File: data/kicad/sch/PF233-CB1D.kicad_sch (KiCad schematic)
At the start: 70 parts, among them M5 5 V 1.5 A switching module, U1 Pico 2 W

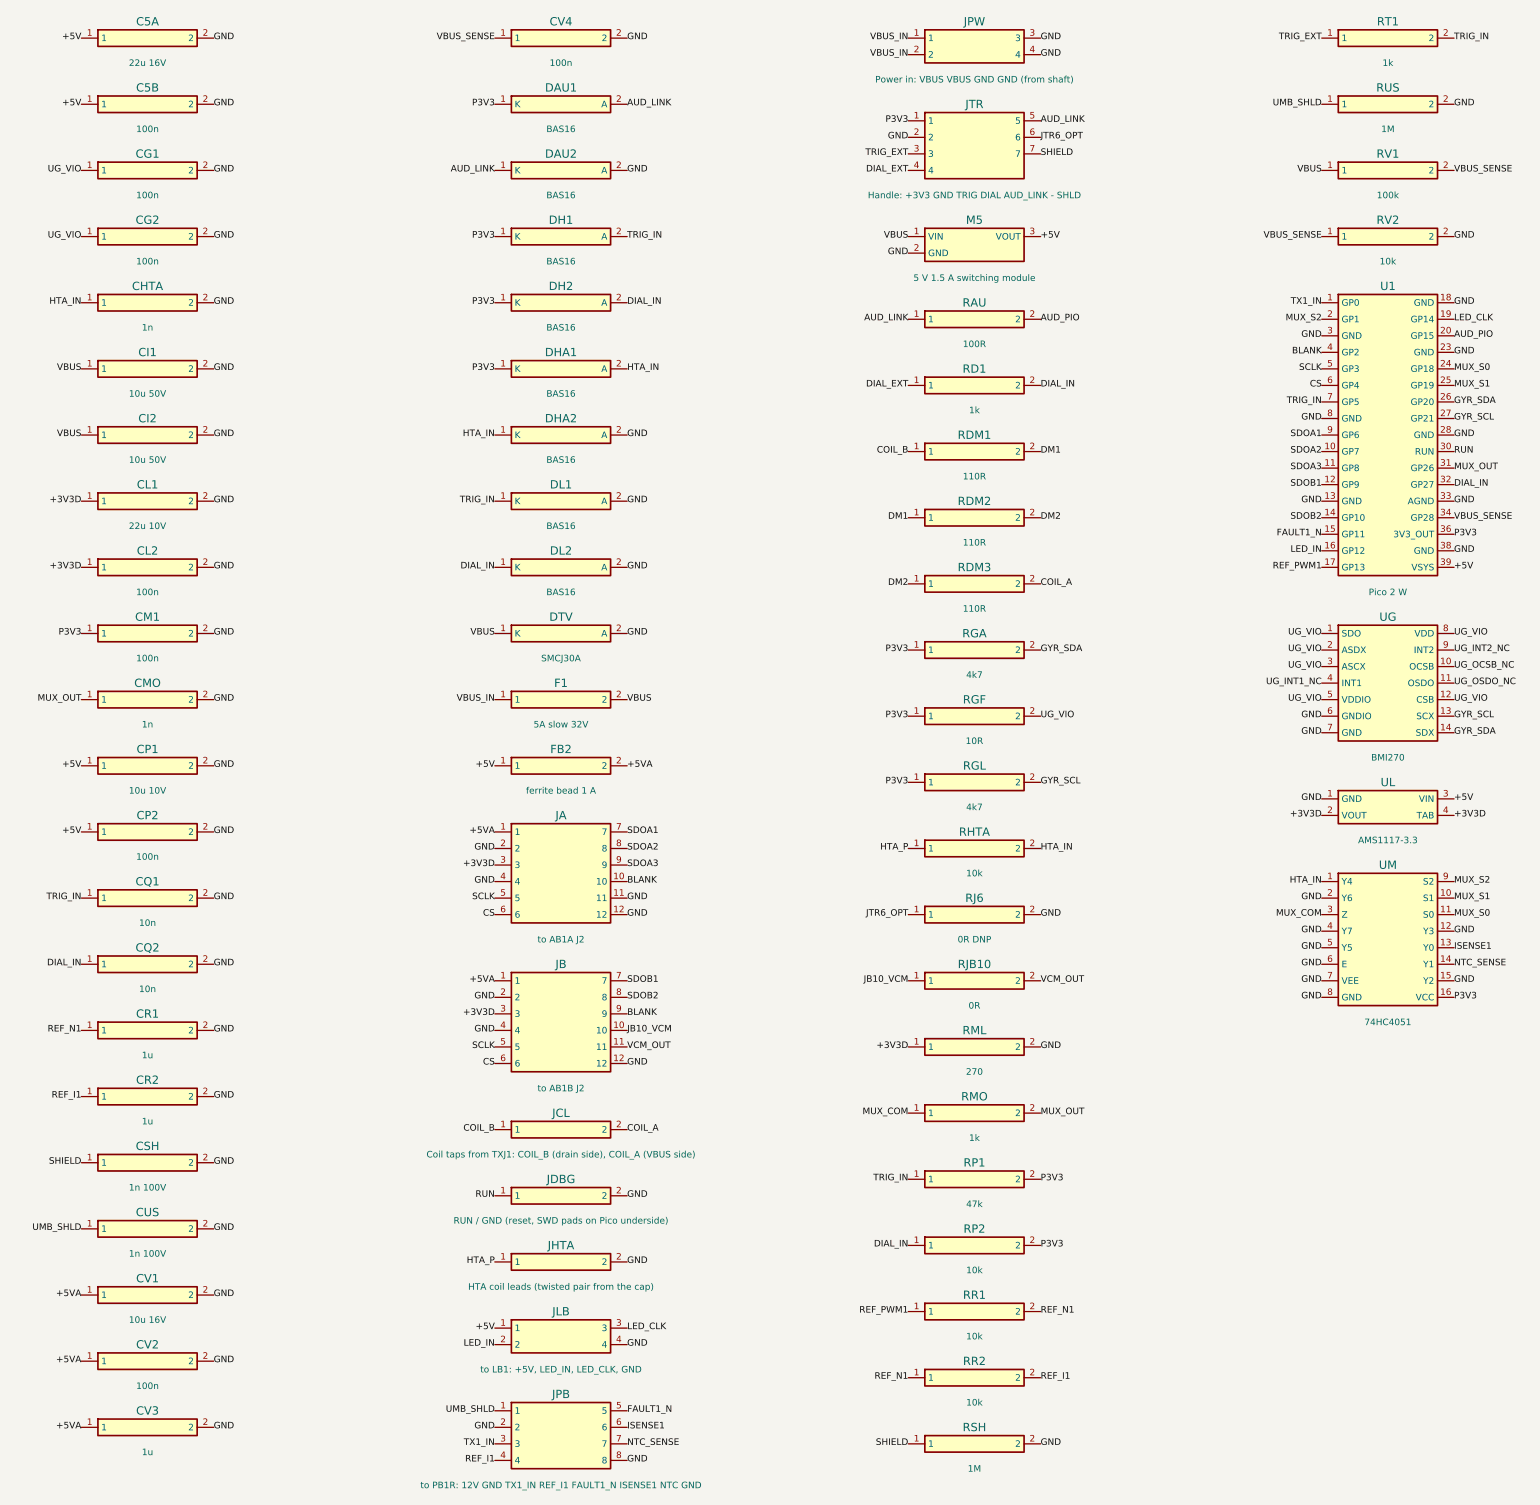
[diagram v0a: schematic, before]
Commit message: WIP (NOT signed off): sign-off outputs with AU1 38 / 38 (exact DRC 0 / 0, all AU1 checks pass); CB1D 45 / 46 (TRIG_EXT open on the 0.125 grid, being re-routed on 0.15)
Co-Authored-By: Claude Opus 5.5 <noreply@anthropic.com>
Claude-Session: https://claude.ai/code/session_01FX4DWSYYjMCFGGA6gmha65
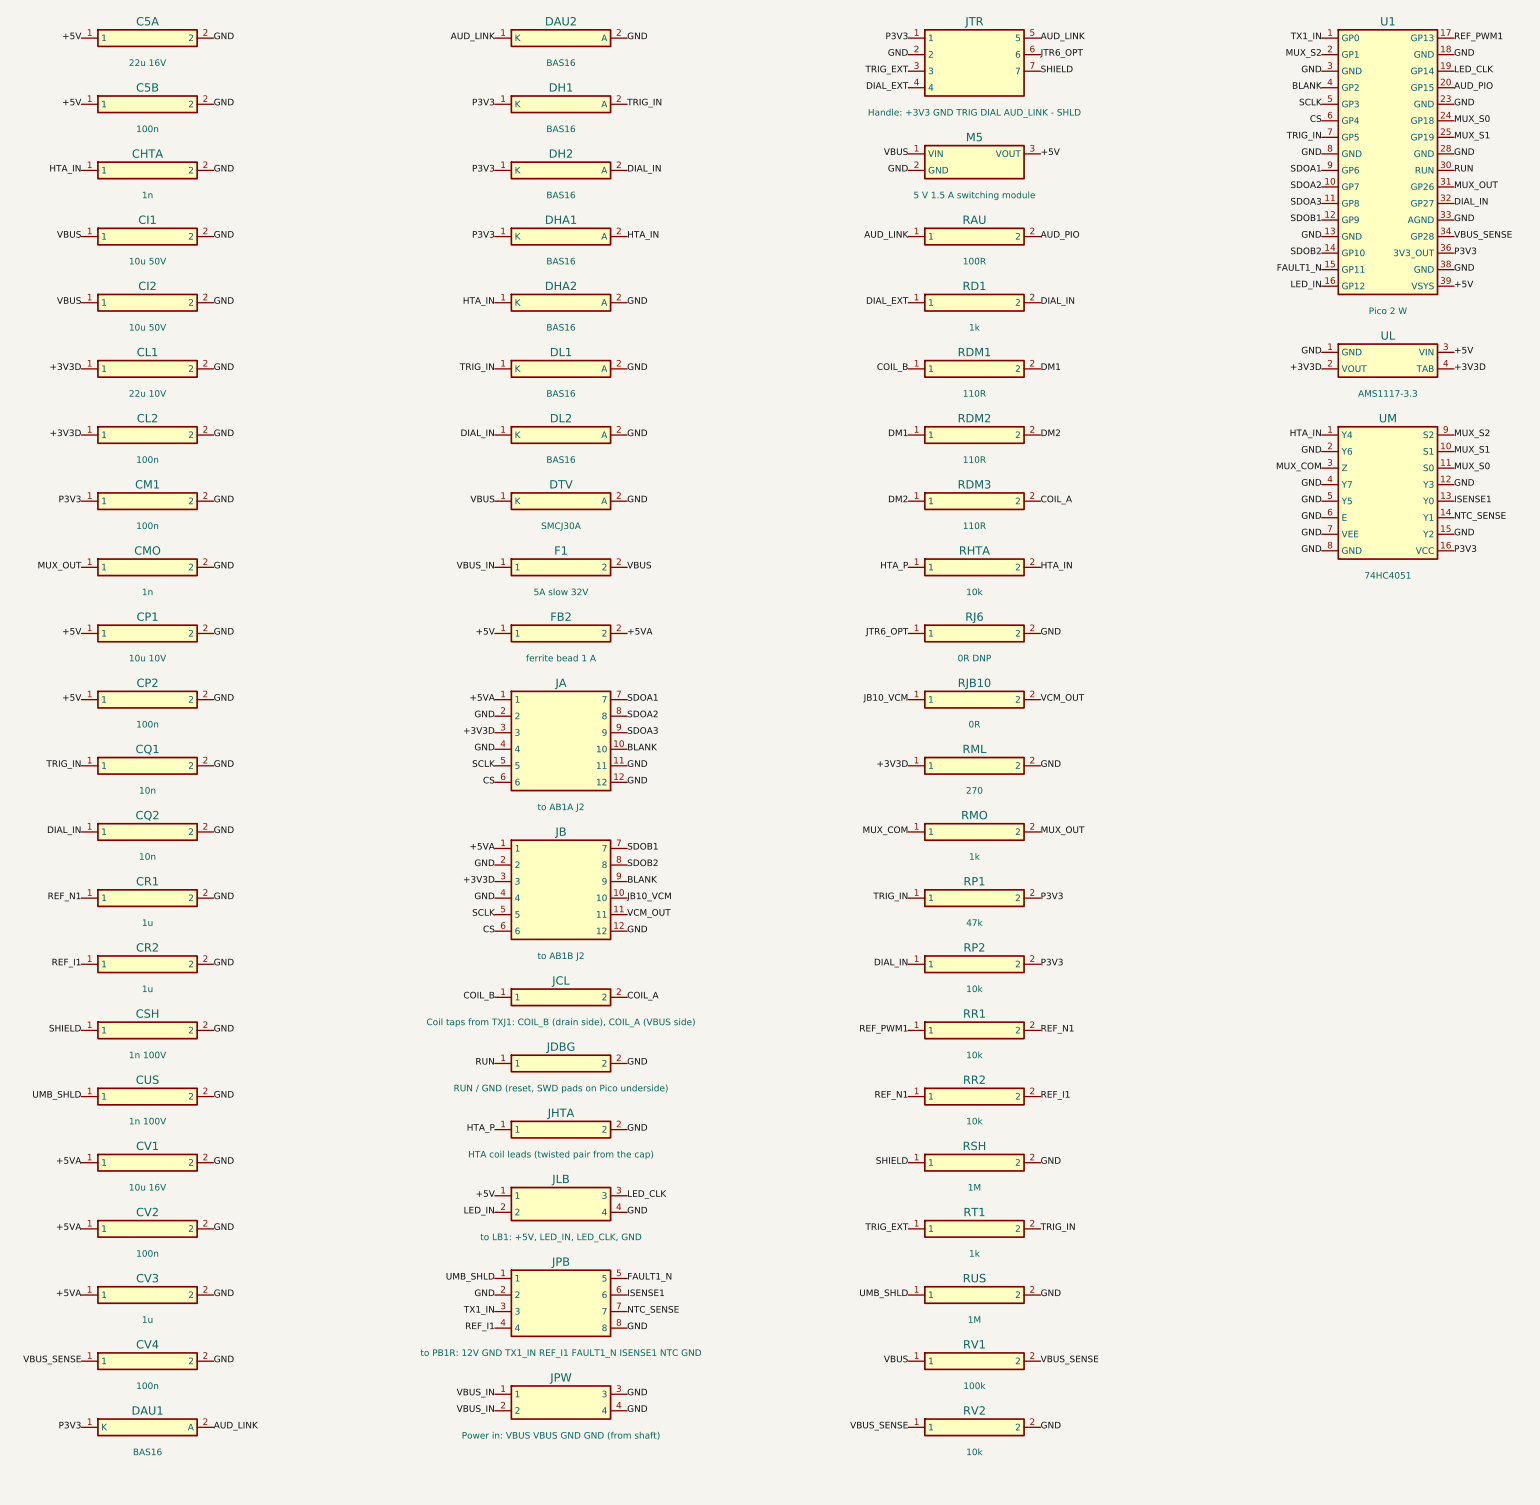
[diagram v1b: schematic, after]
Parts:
- removed CG1: 100n, Capacitor_SMD:C_0603_1608Metric, symbol PF233_auto:CG1
- removed CG2: 100n, Capacitor_SMD:C_0603_1608Metric, symbol PF233_auto:CG2
- removed RGA: 4k7, Resistor_SMD:R_0603_1608Metric, symbol PF233_auto:RGA
- removed RGF: 10R, Resistor_SMD:R_0603_1608Metric, symbol PF233_auto:RGF
- removed RGL: 4k7, Resistor_SMD:R_0603_1608Metric, symbol PF233_auto:RGL
- removed UG: BMI270, PF233:BMI270_LGA-14_2.5x3.0mm, symbol PF233_auto:UG
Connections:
- removed net GYR_SCL: U1.27 (GP21)
- removed net GYR_SDA: U1.26 (GP20)
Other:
- moved on the sheet: CHTA, CI1, CI2, CL1, CL2, CM1, CMO, CP1, CP2, CQ1, CQ2, CR1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

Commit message: Close-out of the output modes / audio / gyro integration: sign-off 76 PASS / 0 FAIL / 4 UNVERIFIED, strict regress 114 / 0, release controls 12 / 12, publish 0 stale
AU1 (36 x 60, 8 layers, gyro moved from CB1D) routed 38 / 38, CB1D-C2 46 / 46, both exact DRC 0 / 0; PB1R-v5 AWG12 solder holes; PM2-B, HB2-B; superseded Gerber sets marked.
Tooling now default: exact-geometry DRC, router fine-pitch keep-out / neck-down / per-board grid, local repair, round checkpoints, non-destructive reset,
interface check, AU1 3-D models with gull-wing leads, counted HV check; pad check traced by the pipeline; process-guard regress row; PROCESS.md / CLAUDE.md / handoff updated.

Co-Authored-By: Claude Opus 5.5 <noreply@anthropic.com>
Claude-Session: https://claude.ai/code/session_01FX4DWSYYjMCFGGA6gmha65
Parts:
- JCL: footprint Connector:Solder_holes_AWG22_1x2_P5.08mm -> Connector:Wire_pads_AWG22_1x2_P5.08mm
- JDBG: footprint Connector:Pin_header_1x2_P2.54mm -> Connector:Wire_pads_1x2_P2.54mm
- JPB: footprint Connector:Pin_header_2x4_P2.54mm -> Connector:Wire_pads_2x4_P2.54mm
- JPW: footprint Connector:Terminal_block_1x4_P5.08mm -> Connector:Wire_pads_1x4_P5.08mm
- JTR: footprint Connector:Pin_header_1x7_P2.54mm -> Connector:Wire_pads_1x7_P2.54mm
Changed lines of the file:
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@@
     (property "Reference" "JCL" (at 93.98 175.26 0) (effects (font (size 1.27 1.27))))
     (property "Value" "Coil taps from TXJ1: COIL_B (drain side), COIL_A (VBUS side)" (at 93.98 181.61 0) (effects (font (size 1.0 1.0))))
-    (property "Footprint" "Connector:Solder_holes_AWG22_1x2_P5.08mm" (at 93.98 177.80 0) (effects (font (size 1.27 1.27)) hide))
+    (property "Footprint" "Connector:Wire_pads_AWG22_1x2_P5.08mm" (at 93.98 177.80 0) (effects (font (size 1.27 1.27)) hide))
     (pin "1")
     (pin "2")
@@
     (property "Reference" "JDBG" (at 93.98 185.42 0) (effects (font (size 1.27 1.27))))
     (property "Value" "RUN / GND (reset, SWD pads on Pico underside)" (at 93.98 191.77 0) (effects (font (size 1.0 1.0))))
-    (property "Footprint" "Connector:Pin_header_1x2_P2.54mm" (at 93.98 187.96 0) (effects (font (size 1.27 1.27)) hide))
+    (property "Footprint" "Connector:Wire_pads_1x2_P2.54mm" (at 93.98 187.96 0) (effects (font (size 1.27 1.27)) hide))
     (pin "1")
     (pin "2")
@@
     (property "Reference" "JPB" (at 93.98 218.44 0) (effects (font (size 1.27 1.27))))
     (property "Value" "to PB1R: 12V GND TX1_IN REF_I1 FAULT1_N ISENSE1 NTC GND" (at 93.98 232.41 0) (effects (font (size 1.0 1.0))))
-    (property "Footprint" "Connector:Pin_header_2x4_P2.54mm" (at 93.98 220.98 0) (effects (font (size 1.27 1.27)) hide))
+    (property "Footprint" "Connector:Wire_pads_2x4_P2.54mm" (at 93.98 220.98 0) (effects (font (size 1.27 1.27)) hide))
     (pin "1")
     (pin "2")
@@
     (property "Reference" "JPW" (at 93.98 236.22 0) (effects (font (size 1.27 1.27))))
     (property "Value" "Power in: VBUS VBUS GND GND (from shaft)" (at 93.98 245.11 0) (effects (font (size 1.0 1.0))))
-    (property "Footprint" "Connector:Terminal_block_1x4_P5.08mm" (at 93.98 238.76 0) (effects (font (size 1.27 1.27)) hide))
+    (property "Footprint" "Connector:Wire_pads_1x4_P5.08mm" (at 93.98 238.76 0) (effects (font (size 1.27 1.27)) hide))
     (pin "1")
     (pin "2")
@@
     (property "Reference" "JTR" (at 157.48 27.94 0) (effects (font (size 1.27 1.27))))
     (property "Value" "Handle: +3V3 GND TRIG DIAL AUD_LINK - SHLD" (at 157.48 41.91 0) (effects (font (size 1.0 1.0))))
-    (property "Footprint" "Connector:Pin_header_1x7_P2.54mm" (at 157.48 30.48 0) (effects (font (size 1.27 1.27)) hide))
+    (property "Footprint" "Connector:Wire_pads_1x7_P2.54mm" (at 157.48 30.48 0) (effects (font (size 1.27 1.27)) hide))
     (pin "1")
     (pin "2")
